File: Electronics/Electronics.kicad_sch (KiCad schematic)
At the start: 21 parts, among them J1 Raspberry_Pi_2_3, J2 HOOK_SWITCH_TERM, J3 DIAL_PULSE_TERM, J4 DIAL_LATCH_TERM, J5 RINGER_BELL, Q1 IRLB8721PBF, U1 TC4422, U2 MT3608

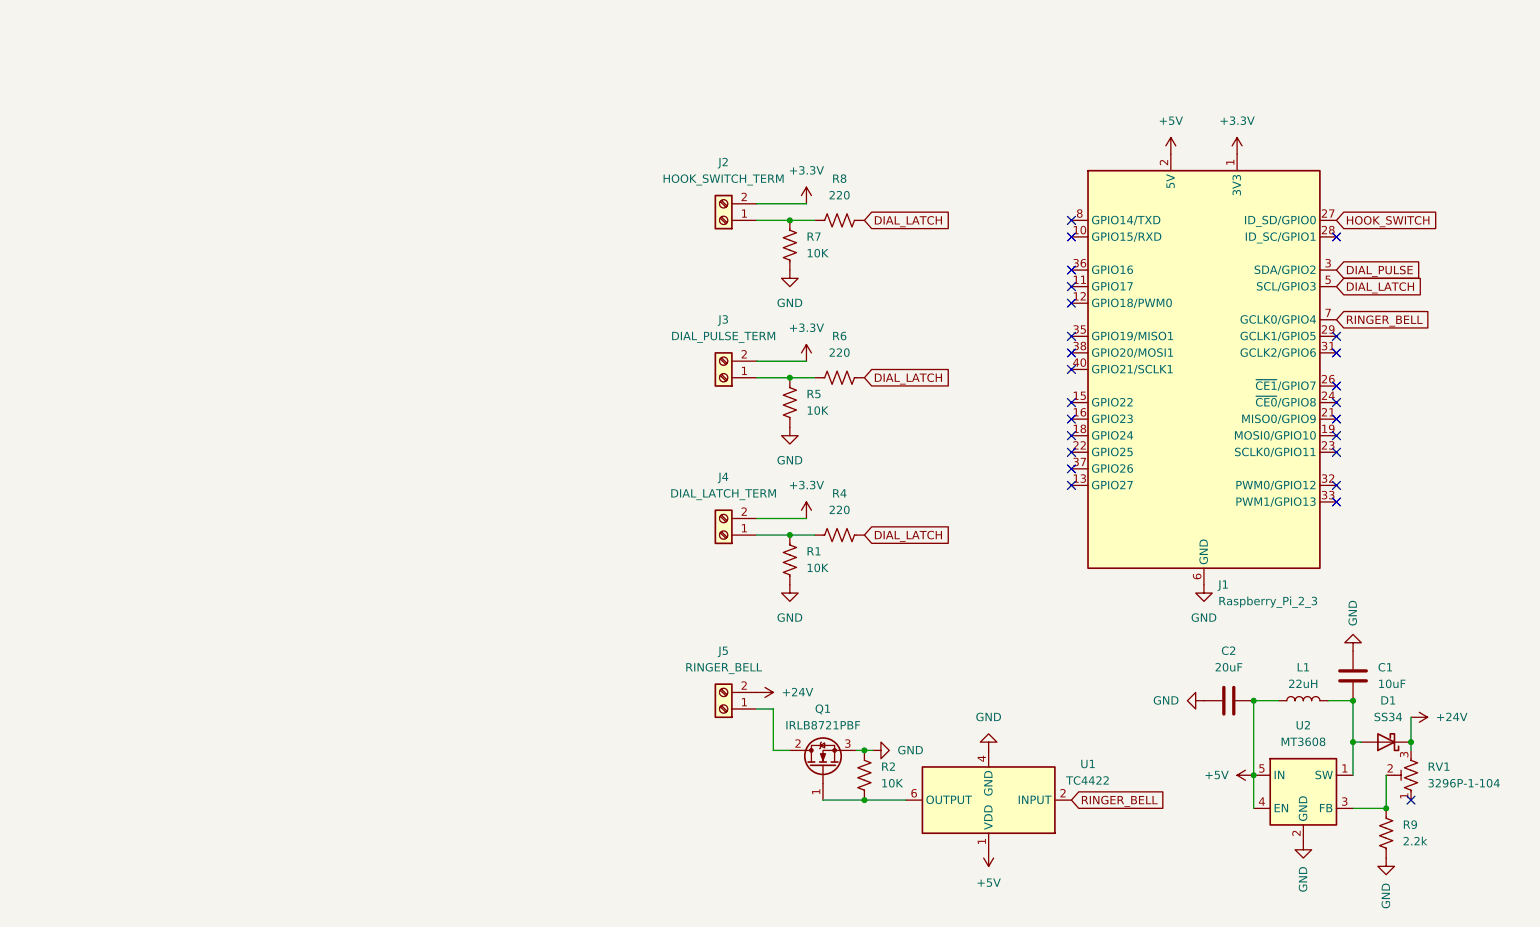
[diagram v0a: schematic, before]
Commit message: Populated the PCB schematic with the components from the final prototype. Preparting for a massive software push.
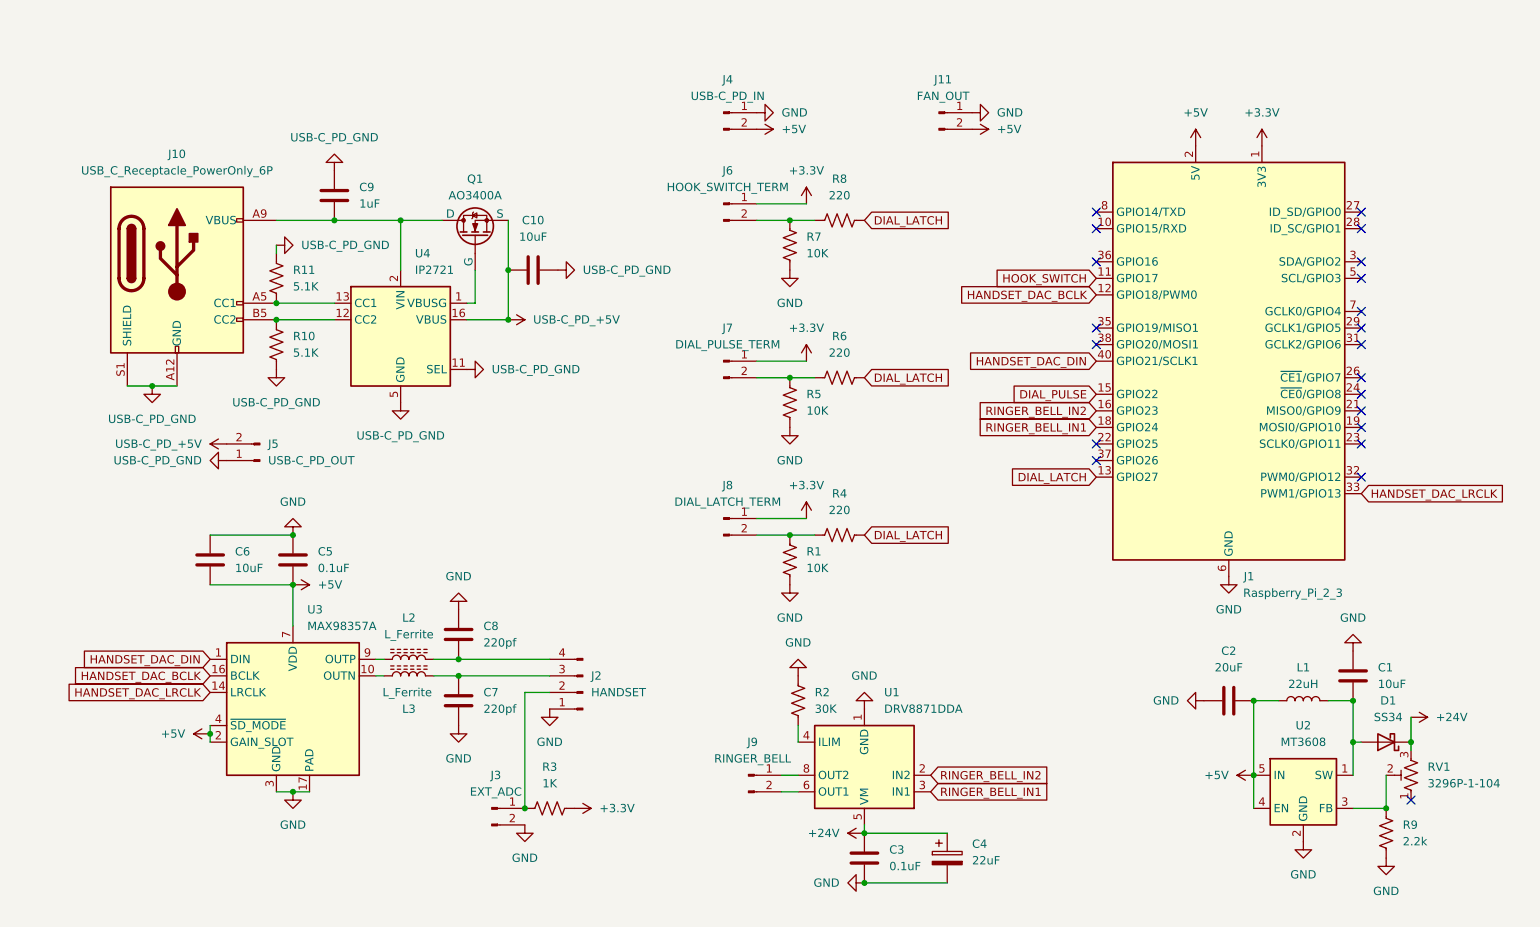
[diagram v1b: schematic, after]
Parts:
- removed J2: HOOK_SWITCH_TERM, symbol Connector:Screw_Terminal_01x02
- removed J3: DIAL_PULSE_TERM, symbol Connector:Screw_Terminal_01x02
- removed J4: DIAL_LATCH_TERM, symbol Connector:Screw_Terminal_01x02
- removed J5: RINGER_BELL, symbol Connector:Screw_Terminal_01x02
- removed Q1: IRLB8721PBF, Package_TO_SOT_THT:TO-220-3_Vertical, symbol Transistor_FET:IRLB8721PBF
- removed U1: TC4422, Package_DIP:DIP-8_W7.62mm, symbol Driver_FET:TC4422
- added C10, C6: 10uF, symbol Device:C
- added C3, C5: 0.1uF, symbol Device:C
- added C4: 22uF, symbol Device:C_Polarized
- added C7, C8: 220pf, symbol Device:C
- added C9: 1uF, symbol Device:C
- added J10: USB_C_Receptacle_PowerOnly_6P, symbol Connector:USB_C_Receptacle_PowerOnly_6P
- added J11: FAN_OUT, symbol Connector:Conn_01x02_Pin
- added J2: HANDSET, symbol Connector:Conn_01x04_Pin
- added J3: EXT_ADC, symbol Connector:Conn_01x02_Pin
- added J4: USB-C_PD_IN, symbol Connector:Conn_01x02_Pin
- added J5: USB-C_PD_OUT, symbol Connector:Conn_01x02_Pin
- added J6: HOOK_SWITCH_TERM, symbol Connector:Conn_01x02_Pin
- added J7: DIAL_PULSE_TERM, symbol Connector:Conn_01x02_Pin
- added J8: DIAL_LATCH_TERM, symbol Connector:Conn_01x02_Pin
- added J9: RINGER_BELL, symbol Connector:Conn_01x02_Pin
- added L2, L3: L_Ferrite, symbol Device:L_Ferrite
- added Q1: AO3400A, symbol Simulation_SPICE:NMOS
- added R10, R11: 5.1K, symbol Device:R_US
- added R3: 1K, symbol Device:R_US
- added U1: DRV8871DDA, Package_SO:Texas_HTSOP-8-1EP_3.9x4.9mm_P1.27mm_EP2.95x4.9mm_Mask2.4x3.1mm_ThermalVias, symbol Driver_Motor:DRV8871DDA
- added U3: MAX98357A, Package_DFN_QFN:TQFN-16-1EP_3x3mm_P0.5mm_EP1.23x1.23mm, symbol Audio:MAX98357A
- added U4: IP2721, Package_SO:TSSOP-16_4.4x5mm_P0.65mm, symbol Interface_USB:IP2721
- R2: value 10K -> 30K
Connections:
- net +24V: now also C3.1, C4.1, U1.5 (VM)
- net +3.3V: now also J6.1 (Pin_1), J7.1 (Pin_1), J8.1 (Pin_1), R3.1
- net +5V: now also C5.2, C6.2, J11.2 (Pin_2), J4.2 (Pin_2), U3.2 (GAIN_SLOT), U3.4 (~{SD_MODE}), U3.7 (VDD), U3.8 (VDD)
- net DIAL_LATCH: now also J1.13 (GPIO27); no longer J1.5 (SCL/GPIO3)
- net DIAL_PULSE: now also J1.15 (GPIO22); no longer J1.3 (SDA/GPIO2)
- net GND: now also C3.2, C4.2, C5.1, C6.1, C7.2, C8.1, J11.1 (Pin_1), J2.1 (Pin_1), J3.2 (Pin_2), J4.1 (Pin_1), U1.1 (GND), U1.7 (GND), U1.9 (GND), U3.11 (GND), U3.15 (GND), U3.17 (PAD), U3.3 (GND)
- net HOOK_SWITCH: now also J1.11 (GPIO17); no longer J1.27 (ID_SD/GPIO0)
- net at R7.2, R8.2: now also J6.2 (Pin_2)
- net at R1.2, R4.2: now also J8.2 (Pin_2)
- net HANDSET_DAC_BCLK: now reaches J1.12 (GPIO18/PWM0)
- net HANDSET_DAC_BCLK: now also U3.16 (BCLK)
- net RINGER_BELL_IN2: now reaches J1.16 (GPIO23)
- net RINGER_BELL_IN2: now also U1.2 (IN2)
- net RINGER_BELL_IN1: now reaches J1.18 (GPIO24)
- net RINGER_BELL_IN1: now also U1.3 (IN1)
- net HANDSET_DAC_LRCLK: now reaches J1.33 (PWM1/GPIO13)
- net HANDSET_DAC_LRCLK: now also U3.14 (LRCLK)
- net HANDSET_DAC_DIN: now reaches J1.40 (GPIO21/SCLK1)
- net HANDSET_DAC_DIN: now also U3.1 (DIN)
- net at R2.1: now also U1.4 (ILIM)
- net at R5.2, R6.2: now also J7.2 (Pin_2)
- net RINGER_BELL: no longer names the net of J1.7 (GCLK0/GPIO4)
- new net: J10.B5 (CC2), R10.2, U4.12 (CC2)
- new net: Q1.2 (G), U4.1 (VBUSG)
- new net: J10.A5 (CC1), R11.1, U4.13 (CC1)
- new net: C9.2, J10.A9 (VBUS), J10.B9 (VBUS), Q1.1 (D), U4.2 (VIN)
- new net: J2.2 (Pin_2), J3.1 (Pin_1), R3.2
- new net: C7.1, J2.3 (Pin_3), L3.2
- new net: C8.2, J2.4 (Pin_4), L2.2
- new net: L3.1, U3.10 (OUTN)
- new net: L2.1, U3.9 (OUTP)
- new net: J9.1 (Pin_1), U1.8 (OUT2)
- new net: J9.2 (Pin_2), U1.6 (OUT1)
- new net USB-C_PD_+5V: C10.1, J5.2 (Pin_2), Q1.3 (S), U4.16 (VBUS)
- new net USB-C_PD_GND: C10.2, C9.1, J10.A12 (GND), J10.B12 (GND), J10.S1 (SHIELD), J5.1 (Pin_1), R10.1, R11.2, U4.11 (SEL), U4.5 (GND)
- no-connect marks 25 -> 21
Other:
- moved on the sheet: J1

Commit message: V1 schematic and PCB are laid out and ready for production
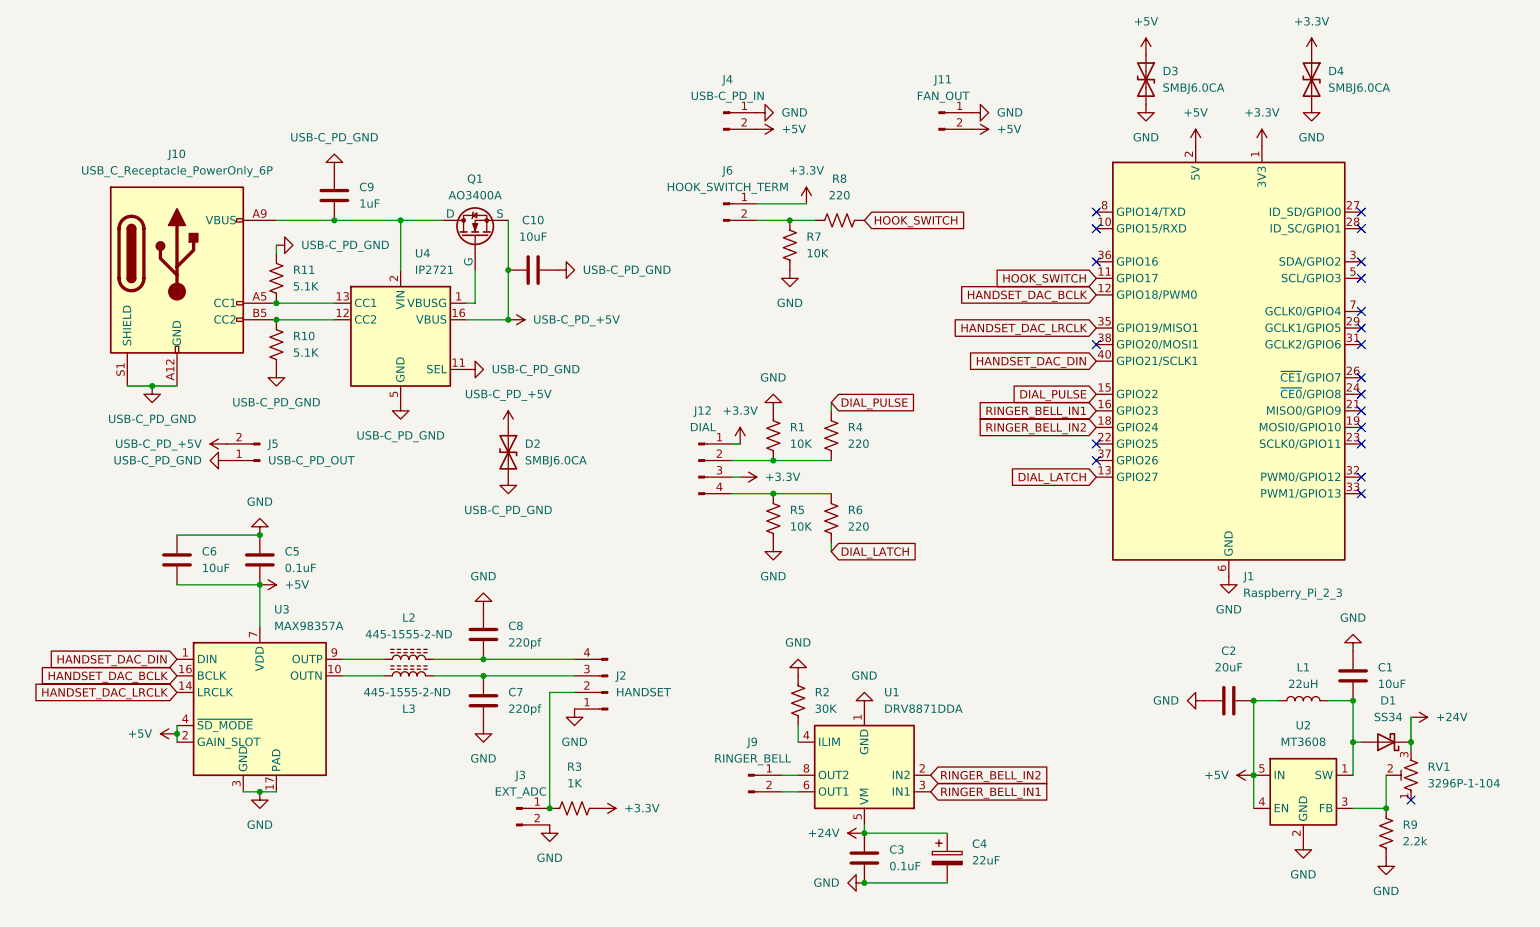
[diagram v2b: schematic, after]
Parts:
- removed J7: DIAL_PULSE_TERM, symbol Connector:Conn_01x02_Pin
- removed J8: DIAL_LATCH_TERM, symbol Connector:Conn_01x02_Pin
- added D2, D3, D4: SMBJ6.0CA, Diode_SMD:D_SMB, symbol Device:D_TVS
- added J12: DIAL, Connector_JST:JST_XH_B4B-XH-A_1x04_P2.50mm_Vertical, symbol Connector:Conn_01x04_Pin
- C1, C10, C2, C3, C4, C5, C6, C7, C8, C9: footprint (none) -> Capacitor_SMD:C_0603_1608Metric
- D1: footprint (none) -> Diode_SMD:D_SMA
- J1: footprint (none) -> Connector_PinSocket_2.54mm:PinSocket_2x20_P2.54mm_Vertical
- J10: footprint (none) -> AdditionalComponents:YIYUAN YTC-TC6-465
- J11: footprint (none) -> Connector_PinHeader_2.54mm:PinHeader_1x02_P2.54mm_Vertical
- J2: footprint (none) -> Connector_JST:JST_XH_B4B-XH-A_1x04_P2.50mm_Vertical
- J3, J4, J5, J6, J9: footprint (none) -> Connector_JST:JST_XH_B2B-XH-A_1x02_P2.50mm_Vertical
- L1: footprint (none) -> AdditionalComponents:CYL104R-22UH
- L2, L3: value L_Ferrite -> 445-1555-2-ND; footprint (none) -> Capacitor_SMD:C_0805_2012Metric
- Q1: footprint (none) -> Package_TO_SOT_SMD:SOT-23
- R1, R10, R11, R2, R3, R4, R5, R6, R7, R8, R9: footprint (none) -> Resistor_SMD:R_0603_1608Metric
- RV1: footprint (none) -> Potentiometer_THT:Potentiometer_Bourns_3296P_Horizontal
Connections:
- net +3.3V: now also D4.1 (A1), J12.1 (Pin_1), J12.3 (Pin_3)
- net +5V: now also D3.1 (A1)
- net DIAL_LATCH: no longer R4.1, R8.1
- net DIAL_PULSE: now also R4.1
- net GND: now also D3.2 (A2), D4.2 (A2)
- net HANDSET_DAC_LRCLK: now also J1.35 (GPIO19/MISO1); no longer J1.33 (PWM1/GPIO13)
- net HOOK_SWITCH: now also R8.1
- net RINGER_BELL_IN1: now also J1.16 (GPIO23); no longer J1.18 (GPIO24)
- net RINGER_BELL_IN2: now also J1.18 (GPIO24); no longer J1.16 (GPIO23)
- net USB-C_PD_+5V: now also D2.1 (A1)
- net USB-C_PD_GND: now also D2.2 (A2)
- net at R1.2, R4.2: now also J12.2 (Pin_2)
- net at R5.2, R6.2: now also J12.4 (Pin_4)
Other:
- moved on the sheet: C5, C6, C7, C8, J2, J3, R1, R3, R4, R5, R6, U3

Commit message: Finalized production exports and now awaiting PCBs to arrive
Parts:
- L1: value 22uH -> YPRH104R-220M; footprint AdditionalComponents:CYL104R-22UH -> AdditionalComponents:YPRH104R-220M
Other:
- moved on the sheet: C2, L1
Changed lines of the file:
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@@
+	(wire
+		(pts
+			(xy 207.01 130.81) (xy 209.55 130.81)
+		)
+		(stroke
+			(width 0)
+			(type default)
+		)
+	)
 	(wire
 		(pts
@@
 	(wire
 		(pts
-			(xy 224.79 130.81) (xy 220.98 130.81)
-		)
-		(stroke
-			(width 0)
-			(type default)
-		)
-	)
-	(wire
-		(pts
-			(xy 209.55 130.81) (xy 213.36 130.81)
+			(xy 224.79 130.81) (xy 217.17 130.81)
 		)
 		(stroke
@@
 	(symbol
 		(lib_id "power:GND")
-		(at 201.93 130.81 270)
+		(at 199.39 130.81 270)
 		(unit 1)
 		(exclude_from_sim no)
@@
 		(dnp no)
 		(property "Reference" "#PWR017"
-			(at 195.58 130.81 0)
+			(at 193.04 130.81 0)
 			(effects
 				(font
@@
 		)
 		(property "Value" "GND"
-			(at 198.12 130.8101 90)
+			(at 195.58 130.8101 90)
 			(effects
 				(font
@@
 		)
 		(property "Footprint" ""
-			(at 201.93 130.81 0)
+			(at 199.39 130.81 0)
 			(effects
 				(font
@@
 		)
 		(property "Datasheet" ""
-			(at 201.93 130.81 0)
+			(at 199.39 130.81 0)
 			(effects
 				(font
@@
 		)
 		(property "Description" "Power symbol creates a global label with name \"GND\" , ground"
-			(at 201.93 130.81 0)
+			(at 199.39 130.81 0)
 			(effects
 				(font
@@
 	(symbol
 		(lib_id "Device:C")
-		(at 205.74 130.81 270)
+		(at 203.2 130.81 270)
 		(unit 1)
 		(exclude_from_sim no)
@@
 		(fields_autoplaced yes)
 		(property "Reference" "C2"
-			(at 205.74 123.19 90)
+			(at 203.2 123.19 90)
 			(effects
 				(font
@@
 		)
 		(property "Value" "20uF"
-			(at 205.74 125.73 90)
+			(at 203.2 125.73 90)
 			(effects
 				(font
@@
 		)
 		(property "Footprint" "Capacitor_SMD:C_0603_1608Metric"
-			(at 201.93 131.7752 0)
+			(at 199.39 131.7752 0)
 			(effects
 				(font
@@
 		)
 		(property "Datasheet" "~"
-			(at 205.74 130.81 0)
+			(at 203.2 130.81 0)
 			(effects
 				(font
@@
 		)
 		(property "Description" "Unpolarized capacitor"
-			(at 205.74 130.81 0)
+			(at 203.2 130.81 0)
 			(effects
 				(font
@@
 	(symbol
 		(lib_id "Device:L")
-		(at 217.17 130.81 90)
+		(at 213.36 130.81 90)
 		(unit 1)
 		(exclude_from_sim no)
@@
 		(fields_autoplaced yes)
 		(property "Reference" "L1"
-			(at 217.17 125.73 90)
-			(effects
-				(font
-					(size 1.27 1.27)
-				)
-			)
-		)
-		(property "Value" "22uH"
-			(at 217.17 128.27 90)
-			(effects
-				(font
-					(size 1.27 1.27)
-				)
-			)
-		)
-		(property "Footprint" "AdditionalComponents:CYL104R-22UH"
-			(at 217.17 130.81 0)
+			(at 213.36 125.73 90)
+			(effects
+				(font
+					(size 1.27 1.27)
+				)
+			)
+		)
+		(property "Value" "YPRH104R-220M"
+			(at 213.36 128.27 90)
+			(effects
+				(font
+					(size 1.27 1.27)
+				)
+			)
+		)
+		(property "Footprint" "AdditionalComponents:YPRH104R-220M"
+			(at 213.36 130.81 0)
 			(effects
 				(font
@@
 		)
 		(property "Datasheet" "~"
-			(at 217.17 130.81 0)
+			(at 213.36 130.81 0)
 			(effects
 				(font
@@
 		)
 		(property "Description" "Inductor"
-			(at 217.17 130.81 0)
-			(effects
-				(font
+			(at 213.36 130.81 0)
+			(effects
+				(font
